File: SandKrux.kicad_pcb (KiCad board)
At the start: 2 copper layers, 147 parts, among them CN1 527450697, CN2 1.25mm-2P socket, J1 Conn_01x02, Q1 S8050, Q2 SI2301CDS-T1-GE3, SW1 TL3330AF130QG, SW2 TL3330AF130QG, SW3 TL3330AF130QG, SW4 TL3330AF130QG, SW5 TL3330AF130QG, U1 K210_C913414, U10 AXP173_C3345106, U2 AXP173, U2 MT9700, U3 MT9700-N, U4 XC6206P182MR_C347373, U5 GD25LQ128EWIGR, U6 TMI7003C, U7 SGM803-TXN3/TR_C5152602, U8 XC6206P302MR_C347375, U9 HX TF-CARD XG8P H1.5, X1 X322526MMB4SI

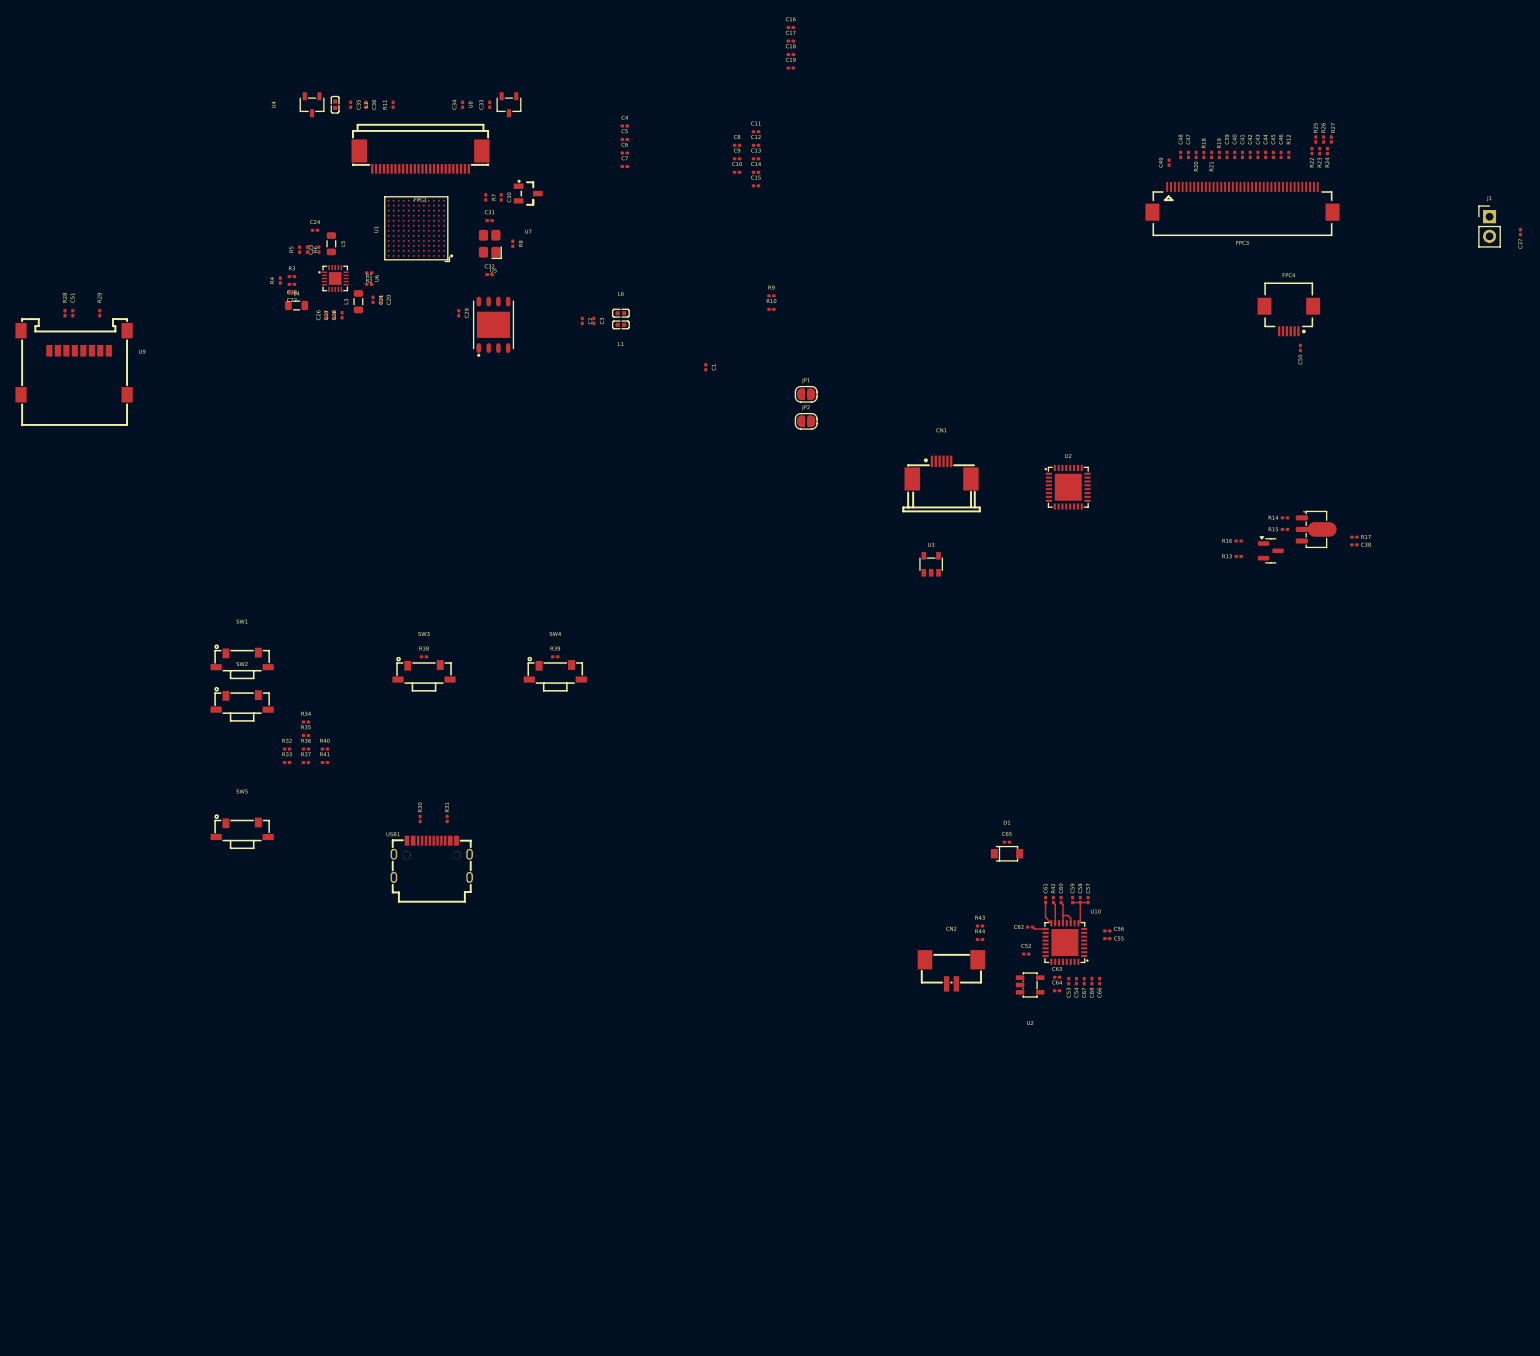
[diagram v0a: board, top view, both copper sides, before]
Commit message: organizacao de componentes, logo, vias e rotas de cirquitos de energia  TROPIC01_chip
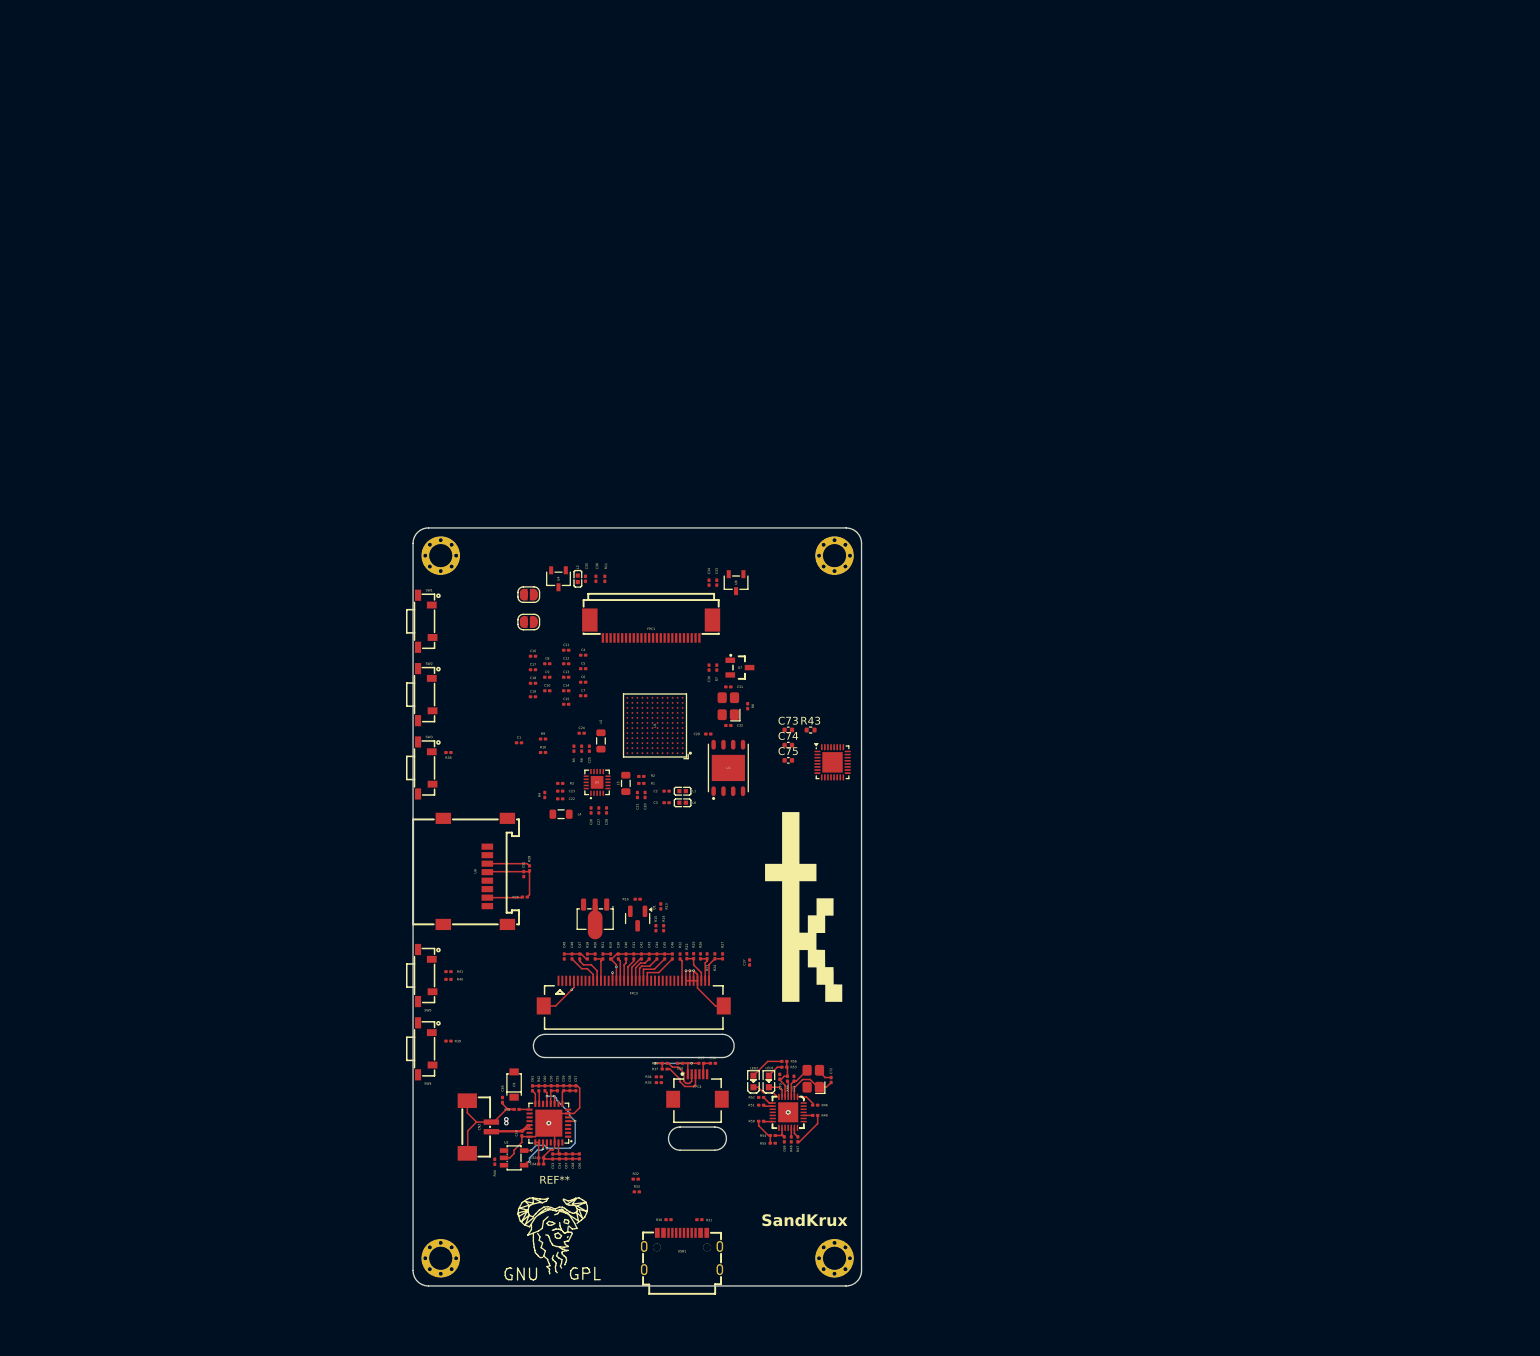
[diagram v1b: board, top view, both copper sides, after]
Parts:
- removed CN1: 527450697, easyeda2kicad:CONN-SMD_527450697
- removed J1: Conn_01x02, Connector_PinHeader_2.54mm:PinHeader_1x02_P2.54mm_Vertical
- removed the U2 at (164.9, 83.5)
- removed U3: MT9700-N, easyeda2kicad:SOT-23-5_L2.9-W1.6-P0.95-LS2.9-BL
- added C69: 10uF, Capacitor_SMD:C_0201_0603Metric, F.Cu at (128.2, 168.0)
- added C70: 10uF, Capacitor_SMD:C_0201_0603Metric, F.Cu at (127.6, 159.9)
- added C71: 18pF, Capacitor_SMD:C_0201_0603Metric, F.Cu at (129.4, 160.1)
- added C72: 18pF, Capacitor_SMD:C_0201_0603Metric, F.Cu at (134.2, 160.3)
- added C73: 100n, Capacitor_SMD:C_0402_1005Metric, F.Cu at (128.7, 115.0)
- added C74: 100n, Capacitor_SMD:C_0402_1005Metric, F.Cu at (128.7, 116.9)
- added C75: 100n, Capacitor_SMD:C_0402_1005Metric, F.Cu at (128.7, 118.9)
- added G***: LOGO, easyeda2kicad:Krux_logo, F.Cu at (130.7, 137.9)
- added H1: ~, PCM_JLCPCB:Hole, 3mm, F.Cu at (134.7, 92.4)
- added H2: ~, PCM_JLCPCB:Hole, 3mm, F.Cu at (83.7, 92.4)
- added H3: ~, PCM_JLCPCB:Hole, 3mm, F.Cu at (83.7, 183.4)
- added H4: ~, PCM_JLCPCB:Hole, 3mm, F.Cu at (134.7, 183.4)
- added IC1: TROPIC01_chip, easyeda2kicad:QFN-32-1EP_4x4mm_P0.4mm_EP2.65x2.65mm, F.Cu at (134.4, 119.2)
- added LED1: KT-0603R, easyeda2kicad:LED0603-RD, F.Cu at (126.2, 160.5)
- added LED2: KT-0603R, easyeda2kicad:LED0603-RD, F.Cu at (124.2, 160.5)
- added R45: 1.5, Resistor_SMD:R_0201_0603Metric, F.Cu at (128.6, 160.1)
- added R46: 1.5K, Resistor_SMD:R_0201_0603Metric, F.Cu at (132.2, 163.6)
- added R47: 22R, Resistor_SMD:R_0201_0603Metric, F.Cu at (129.9, 168.0)
- added R48: 22R, Resistor_SMD:R_0201_0603Metric, F.Cu at (129.1, 168.0)
- added R49: 1.5K, Resistor_SMD:R_0201_0603Metric, F.Cu at (132.2, 164.9)
- added R50: 22R, Resistor_SMD:R_0201_0603Metric, F.Cu at (125.2, 165.6)
- added R51: 22R, Resistor_SMD:R_0201_0603Metric, F.Cu at (125.2, 163.6)
- added R52: 22R, Resistor_SMD:R_0201_0603Metric, F.Cu at (125.2, 162.6)
- added R53: 5.1K, Resistor_SMD:R_0201_0603Metric, F.Cu at (128.2, 158.6)
- added R54: 10K, Resistor_SMD:R_0201_0603Metric, F.Cu at (126.7, 167.5)
- added R55: NC, Resistor_SMD:R_0201_0603Metric, F.Cu at (126.7, 168.5)
- added R56: 5.1K, Resistor_SMD:R_0201_0603Metric, F.Cu at (128.2, 157.9)
- added REF**: Symbol_GNU-Logo_SilkscreenTop, Symbol:Symbol_GNU-Logo_SilkscreenTop, F.Cu at (98.4, 179.3)
- added U11: GD32F150G8U6, easyeda2kicad:WQFN-28_L4.0-W4.0-P0.40-BL-EP, F.Cu at (128.7, 164.5)
- added X2: X322526MMB4SI, PCM_JLCPCB:CRYSTAL-SMD_4P-L3.2-W2.5-BL, F.Cu at (131.9, 160.1)
- R43: value 0R -> 47k; footprint Resistor_SMD:R_0201_0603Metric -> Resistor_SMD:R_0402_1005Metric
- moved C37 137.5 mm to (123.7, 145.1), turned to 90 degrees
- moved R26 133.1 mm to (117.3, 144.3)
- moved R25 133.0 mm to (116.4, 144.3)
- moved R22 132.0 mm to (115.5, 144.3)
- moved R27 131.9 mm to (120.2, 144.3)
- moved R23 131.0 mm to (118.2, 144.3)
- moved R24 131.0 mm to (119.2, 144.3)
- moved R18 131.0 mm to (102.7, 144.3)
- moved C39 130.3 mm to (106.7, 144.3)
- moved C40 130.3 mm to (107.7, 144.3)
- moved C41 130.3 mm to (108.7, 144.3)
- moved C42 130.3 mm to (109.7, 144.3)
- moved C43 130.3 mm to (110.7, 144.3)
- moved C44 130.3 mm to (111.7, 144.3)
- moved C45 130.3 mm to (112.7, 144.3)
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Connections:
- net /0V9 renamed /k210/0V9
- net /0v9 renamed /k210/0v9
- net /1V8 renamed /k210/1V8
- net /26M_OUT renamed /k210/26M_OUT
- net /5v renamed /k210/5v
- net /AFGND renamed /k210/AFGND
- net /AFVCC renamed /k210/AFVCC
- net /BOOT renamed /k210/BOOT
- net /CMOS-AVDD renamed /k210/CMOS-AVDD
- net /CMOS-DVDD renamed /k210/CMOS-DVDD
- net /DVP_D0 renamed /k210/DVP_D0
- net /DVP_D1 renamed /k210/DVP_D1
- net /DVP_D2 renamed /k210/DVP_D2
- net /DVP_D3 renamed /k210/DVP_D3
- net /DVP_D4 renamed /k210/DVP_D4
- net /DVP_D5 renamed /k210/DVP_D5
- net /DVP_D6 renamed /k210/DVP_D6
- net /DVP_D7 renamed /k210/DVP_D7
- net /DVP_HSYNC renamed /k210/DVP_HSYNC
- net /DVP_PCLK renamed /k210/DVP_PCLK
- net /DVP_PWDN renamed /k210/DVP_PWDN
- net /DVP_RST renamed /k210/DVP_RST
- net /DVP_SCL renamed /k210/DVP_SCL
- net /DVP_SDA renamed /k210/DVP_SDA
- net /DVP_VSYNC renamed /k210/DVP_VSYNC
- net /DVP_XCLK renamed /k210/DVP_XCLK
- net /F_CLK renamed /k210/F_CLK
- net /F_CS renamed /k210/F_CS
- net /F_D0 renamed /k210/F_D0
- net /F_D1 renamed /k210/F_D1
- net /F_D2 renamed /k210/F_D2
- net /F_D3 renamed /k210/F_D3
- net /IO_10 renamed /k210/IO_10
- net /IO_11 renamed /k210/IO_11
- net /IO_12 renamed /k210/IO_12
- net /IO_13 renamed /k210/IO_13
- net /IO_14 renamed /k210/IO_14
- net /IO_15 renamed /k210/IO_15
- net /IO_17 renamed /k210/IO_17
- net /IO_18 renamed /k210/IO_18
- net /IO_19 renamed /k210/IO_19
- net /IO_20 renamed /k210/IO_20
- net /IO_21 renamed /k210/IO_21
- net /IO_22 renamed /k210/IO_22
- net /IO_23 renamed /k210/IO_23
- net /IO_24 renamed /k210/IO_24
- net /IO_25 renamed /k210/IO_25
- net /IO_26 renamed /k210/IO_26
- net /IO_27 renamed /k210/IO_27
- net /IO_28 renamed /k210/IO_28
- net /IO_29 renamed /k210/IO_29
- net /IO_30 renamed /k210/IO_30
- net /IO_31 renamed /k210/IO_31
- net /IO_32 renamed /k210/IO_32
- net /IO_33 renamed /k210/IO_33
- net /IO_34 renamed /k210/IO_34
- net /IO_35 renamed /k210/IO_35
- net /IO_6 renamed /k210/IO_6
- net /IO_7 renamed /k210/IO_7
- net /IO_8 renamed /k210/IO_8
- net /IO_9 renamed /k210/IO_9
- net /JTAG_TCK renamed /k210/JTAG_TCK
- net /JTAG_TDI renamed /k210/JTAG_TDI
- net /JTAG_TDO renamed /k210/JTAG_TDO
- net /JTAG_TMS renamed /k210/JTAG_TMS
- net /SPI0_D0 renamed /k210/SPI0_D0
- net /SPI0_D1 renamed /k210/SPI0_D1
- net /SPI0_D2 renamed /k210/SPI0_D2
- net /SPI0_D3 renamed /k210/SPI0_D3
- net /SPI0_D4 renamed /k210/SPI0_D4
- net /SPI0_D5 renamed /k210/SPI0_D5
- net /SPI0_D7 renamed /k210/SPI0_D7
- net /SPI0_D8 renamed /k210/SPI0_D8
- net /UARTHS_RX renamed /k210/UARTHS_RX
- net /UARTHS_TX renamed /k210/UARTHS_TX
- net /Vadj renamed /k210/Vadj
- net /Vb renamed /k210/Vb
- net /XIN renamed /k210/XIN
- net /XOUT renamed /k210/XOUT
- C30 pad 2: /RST -> /k210/RST
- C37 pad 1: /<NO NET> -> /3V3
- C4 pad 2: /<NO NET> -> /k210/<NO NET>
- C49 pad 1: /<NO NET> -> /3V3
- C5 pad 2: /<NO NET> -> /k210/<NO NET>
- C50 pad 1: /<NO NET> -> /3V3
- C51 pad 2: /<NO NET> -> /3V3
- C53 pad 2: /<NO NET> -> /3V3
- C54 pad 2: /<NO NET> -> /3V3
- C6 pad 2: /<NO NET> -> /k210/<NO NET>
- C66 pad 2: /<NO NET> -> /3V3
- C67 pad 2: /<NO NET> -> /3V3
- C68 pad 2: /<NO NET> -> /3V3
- C7 pad 2: /<NO NET> -> /k210/<NO NET>
- FPC4 pad 1: /<NO NET> -> /3V3
- JP2 pad 1: /<NO NET> -> /k210/<NO NET>
- L2 pad 2: /<NO NET> -> /k210/<NO NET>
- Q2 pad 2: /<NO NET> -> /3V3
- R15 pad 2: /<NO NET> -> /3V3
- R17 pad 1: /<NO NET> -> /3V3
- R28 pad 2: /<NO NET> -> /3V3
- R29 pad 2: /<NO NET> -> /3V3
- R32 pad 2: /<NO NET> -> /3V3
- R33 pad 2: /<NO NET> -> /3V3
- R34 pad 2: /<NO NET> -> /3V3
- R35 pad 2: /<NO NET> -> /3V3
- R36 pad 1: /<NO NET> -> /3V3
- R37 pad 1: /<NO NET> -> /3V3
- R38 pad 1: /<NO NET> -> /3V3
- R39 pad 1: /<NO NET> -> /3V3
- R40 pad 2: /<NO NET> -> /3V3
- R43 pad 1: GND -> /SPI_MISO
- R43 pad 2: GND -> VCC
- R7 pad 2: /RST -> /k210/RST
- U1 pad A1: /LCD_RST -> /k210/LCD_RST
- U1 pad A2: /LCD_CS -> /k210/LCD_CS
- U1 pad B1: /LCD_WR -> /k210/LCD_WR
- U1 pad B2: /LCD_DC -> /k210/LCD_DC
- U1 pad C5: /<NO NET> -> /k210/<NO NET>
- U1 pad C7: /<NO NET> -> /k210/<NO NET>
- U1 pad C8: /<NO NET> -> /k210/<NO NET>
- U1 pad D10: /<NO NET> -> /k210/<NO NET>
- U1 pad G10: /<NO NET> -> /k210/<NO NET>
- U1 pad H10: /<NO NET> -> /k210/<NO NET>
- U1 pad M1: /RST -> /k210/RST
- U10 pad 31: /<NO NET> -> /3V3
- U7 pad 2: /RST -> /k210/RST
- U7 pad 3: /<NO NET> -> /k210/<NO NET>
- U8 pad 3: /<NO NET> -> /k210/<NO NET>
- U9 pad 4: /<NO NET> -> /3V3
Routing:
- net GND: track 0.00 -> 84.6 mm, vias 0 -> 9
- net /3V3: track 0.00 -> 32.8 mm, vias 0 -> 2
- net /IPSOUT: track 4.57 -> 20.0 mm, vias 0 -> 5
- net /VBAT: track 0.00 -> 12.2 mm
- net /24M_IN: track 0.00 -> 7.06 mm
- net /I2C_SCL: track 0.00 -> 6.28 mm
- net /I2C_SDA: track 0.00 -> 5.90 mm
- net /SPI1_MOSI: track 0.00 -> 5.58 mm
- net /LCD_D7: track 0.00 -> 5.04 mm
- net /LCD_D6: track 0.00 -> 4.80 mm
- net /24M_OUT: track 0.00 -> 4.71 mm
- net /USBDP_GD32: track 0.00 -> 4.60 mm
- net Net-(U9-DAT0): track 0.00 -> 4.57 mm
- net /EXTEN: track 0.00 -> 4.45 mm, vias 0 -> 2
- net Net-(LED2-A): track 0.00 -> 4.45 mm
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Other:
- board outline added: 58.1 x 98.2 mm
- board text added: "SandKrux"

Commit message: vias e rotas de componentes + atualizacao de logo
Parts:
- added G***: LOGO, easyeda2kicad:SandKrux, F.Cu at (97.2, 182.2)
- moved REF** 28.8 mm to (127.2, 179.8)
- moved U4 26.1 mm to (125.0, 94.7), turned to 180 degrees
- moved L2 26.1 mm to (127.5, 94.9)
- moved U8 23.5 mm to (98.5, 94.5), turned to 0 degrees
- moved C35 20.1 mm to (122.5, 94.7), turned to -90 degrees
- moved C36 17.8 mm to (121.5, 94.7), turned to -90 degrees
- moved C33 17.5 mm to (101.9, 94.6)
- moved C34 17.5 mm to (100.9, 94.6)
- moved R11 15.4 mm to (120.2, 94.7), turned to -90 degrees
- moved C73 13.5 mm to (130.0, 101.5)
- moved C74 13.5 mm to (130.0, 103.5)
- moved C75 13.5 mm to (130.0, 105.4)
- moved R43 13.5 mm to (132.9, 101.5)
- moved IC1 13.5 mm to (134.8, 105.7)
- moved Q2 8.05 mm to (111.7, 139.0)
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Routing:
- net GND: track 84.6 -> 191.6 mm, vias 9 -> 18
- net /5V_USB: track 0.00 -> 67.3 mm
- net /k210/0V9: track 0.00 -> 45.3 mm, vias 0 -> 9
- net /3V3: track 32.8 -> 57.8 mm, vias 2 -> 3
- net /VCC_1V83V3: track 3.93 -> 25.6 mm, vias 0 -> 2
- net /k210/CMOS-DVDD: track 0.00 -> 17.4 mm
- net /k210/CMOS-AVDD: track 0.00 -> 13.1 mm
- net /k210/DVP_XCLK: track 0.00 -> 12.7 mm, vias 0 -> 2
- net /k210/1V8: track 0.00 -> 12.5 mm, vias 0 -> 4
- net /k210/DVP_SDA: track 0.00 -> 12.1 mm, vias 0 -> 2
- net /k210/DVP_PCLK: track 0.00 -> 12.0 mm, vias 0 -> 2
- net Net-(Q1-C): track 0.00 -> 11.8 mm, vias 0 -> 2
- net /k210/DVP_RST: track 0.00 -> 11.4 mm, vias 0 -> 2
- net /LCD_BACKLIGHT: track 0.00 -> 11.2 mm
- net /k210/DVP_PWDN: track 0.00 -> 11.2 mm, vias 0 -> 2
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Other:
- board text added: "v.0"
- board text removed: "SandKrux"

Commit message: detalhamento do PCIE-67P42H
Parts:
- added U12: PCIE-67P42H, easyeda2kicad:PCIE-SMD_75P-P0.50_HYC01B-05NGFF-420, F.Cu at (57.5, 136.2)
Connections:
- net /k210/JTAG_TCK renamed /k210/IO_0
- net /k210/JTAG_TDI renamed /k210/IO_1
- net /k210/JTAG_TDO renamed /k210/IO_3
- net /k210/JTAG_TMS renamed /k210/IO_2
- U1 pad H11: /k210/UARTHS_RX -> /k210/IO_4
- U1 pad H12: /k210/UARTHS_TX -> /k210/IO_5
